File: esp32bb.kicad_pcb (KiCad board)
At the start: 2 copper layers, 43.2 x 61 mm, 33 parts, among them CON1 Micro_SD_Card, IC1 FT232RQ, J1 CONN_01X18, P1 CONN_01X17, P3 USB_OTG, Q1 MMBT3904, Q2 MMBT3904, SW1 SWITCH_SPST, SW2 SWITCH_SPST, U1 ESP32-WROOM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

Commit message: Update schema to use CP2102 and NCP1117DT33 and remove SD card holder
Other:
- board text added: "D00 PULL UP"
- board text removed: "D01 PULL UP"
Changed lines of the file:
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@@
     (effects (font (size 1.1 1.1) (thickness 0.2)))
   )
-  (gr_text "D01\nPULL\nUP" (at 161.417 118.237) (layer B.SilkS)
+  (gr_text "D00\nPULL\nUP" (at 161.417 118.237) (layer B.SilkS)
     (effects (font (size 0.7 0.7) (thickness 0.175)) (justify right mirror))
   )

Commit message: Update pcb for rev2.0
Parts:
- removed CON1: Micro_SD_Card, Connectors_Hirose:microSD_Card_Receptacle_Hirose_DM3AT-SF-PEJM5
- removed IC1: FT232RQ, ftdi232rq:FR232RQ
- removed J1: CONN_01X18, common:Pin_Header_Straight_1x18_Pitch2.54mm
- removed R10, R11, R12, R13, R8, R9: 10K, Resistors_SMD:R_0603
- added C1: 1nf, Capacitors_SMD:C_0603, F.Cu at (171.8, 101.8)
- added C7: 1nf, Capacitors_SMD:C_0603, F.Cu at (171.8, 94.6)
- added C8: 100uf, Capacitors_SMD:C_1206, F.Cu at (169.8, 106.3)
- added P2: CONN_01X17, common:Pin_Header_Straight_1x17_Pitch2.54mm, B.Cu at (190.5, 71.1)
- added P3: USB_OTG, usb_micro_b:USB_MICRO_B-HIROSE-ZX62R-B-5P, F.Cu at (167.6, 115.3)
- added U3: CP2102, Housings_DFN_QFN:QFN-28-1EP_5x5mm_Pitch0.5mm, F.Cu at (180.7, 100.4)
- D2: value D02 -> D05
- U2: value NJU7223DL1-33 -> NCP1117ST33T3G; footprint TO_SOT_Packages_SMD:TO-252-2Lead -> TO_SOT_Packages_SMD:SOT-223
- moved SW2 24.9 mm to (159.2, 118.8)
- moved SW1 24.9 mm to (184.1, 118.8)
- moved C4 23.5 mm to (162.0, 106.3)
- moved C5 23.5 mm to (162.0, 103.7)
- moved U2 19.5 mm to (164.1, 98.2)
- moved REF*** 18.6 mm to (157.4, 110.5)
- moved C2 16.3 mm to (165.4, 106.3), turned to 180 degrees
- moved C3 16.3 mm to (165.4, 103.7), turned to 180 degrees
- moved D1 12.8 mm to (174.5, 106.3), turned to 0 degrees
- moved D2 11.3 mm to (177.7, 119.1)
- moved R5 8.13 mm to (180.8, 95.4)
- moved R6 7.46 mm to (173.7, 98.1)
- moved Q1 6.11 mm to (174.5, 101.8)
- moved G*** 5.80 mm to (171.6, 65.9)
- moved U1 5.62 mm to (171.6, 76.5)
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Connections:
- C6 pad 1: Net-(C6-Pad1) -> GND
- C6 pad 2: GND -> Net-(C6-Pad2)
- P1 pad 17: +3V3 -> VCC
- R7 pad 1: IO2 -> IO5
- U1 pad 17: SD2 -> Net-(U1-Pad17)
- U1 pad 18: SD3 -> Net-(U1-Pad18)
- U1 pad 19: SD_CMD -> Net-(U1-Pad19)
- U1 pad 20: SD_CLK -> Net-(U1-Pad20)
- U1 pad 21: SD0 -> Net-(U1-Pad21)
- U1 pad 22: SD1 -> Net-(U1-Pad22)
- U2 pad 1: +3V3 -> GND
- U2 pad 2: VCC -> +3V3
- U2 pad 3: GND -> VCC
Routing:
- net GND: track 218.3 -> 291.8 mm, vias 11 -> 24
- net SD1: track 39.0 -> 0.00 mm
- net +3V3: track 151.9 -> 113.5 mm, vias 7 -> 4
- net SD0: track 36.4 -> 0.00 mm, vias 2 -> 0
- net SD_CLK: track 32.6 -> 0.00 mm, vias 2 -> 0
- net SD_CMD: track 28.0 -> 0.00 mm, vias 2 -> 0
- net SD3: track 26.6 -> 0.00 mm, vias 2 -> 0
- net SD2: track 25.5 -> 0.00 mm, vias 2 -> 0
- net Net-(P3-Pad4): track 0.00 -> 14.9 mm, vias 0 -> 2
- net IO2: track 39.5 -> 27.2 mm, vias 3 -> 0
- net IO5: track 21.3 -> 33.4 mm, vias 0 -> 1
- net D+: track 18.4 -> 29.1 mm, vias 0 -> 2
- net D-: track 18.5 -> 27.6 mm, vias 0 -> 2
- net IO0(boot): track 64.6 -> 57.5 mm, vias 4 -> 3
- net (no net): track 2.72 -> 9.74 mm, vias 0 -> 5
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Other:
- outline, holes or cut-outs redrawn
- board text added: "D00"
- board text added: "Rev 2.0"
- board text added: "VIN"
- board text removed: "D00 PULL UP"
- board text removed: "Rev 1.4"
- board text removed: "VCC"

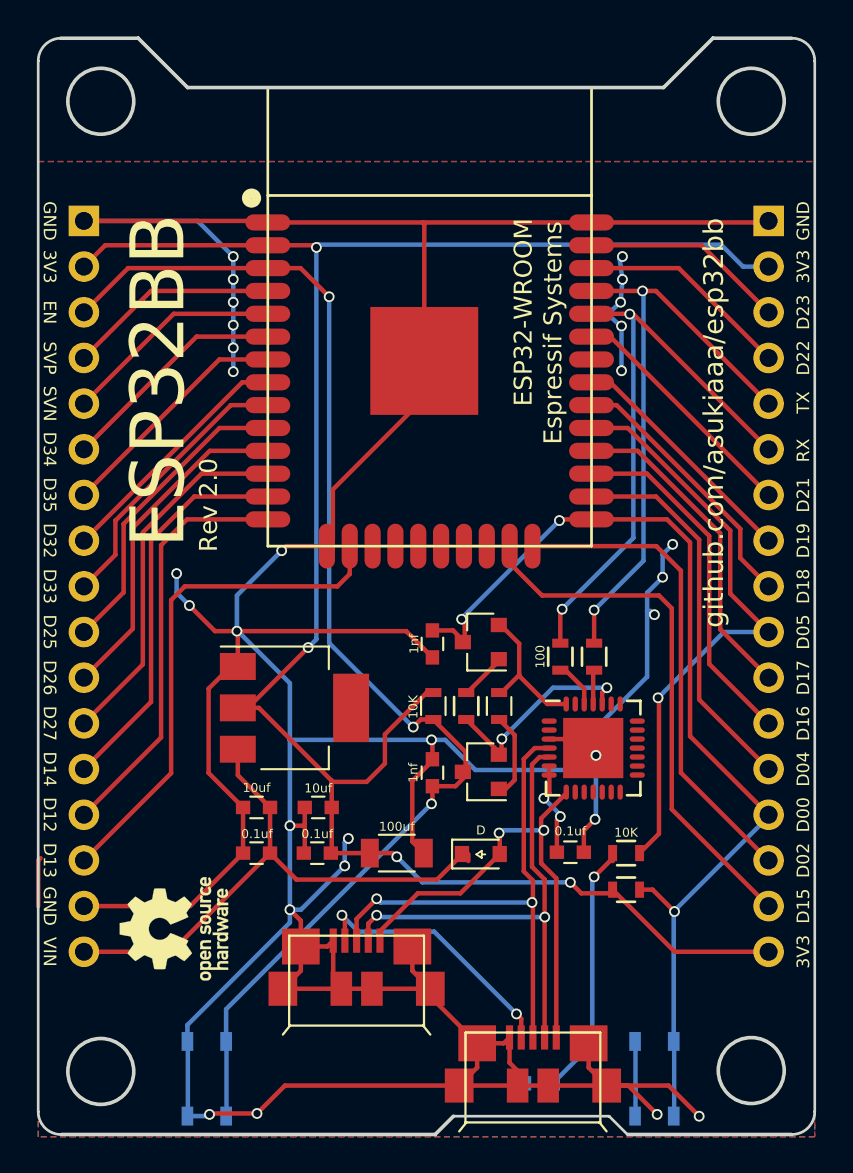
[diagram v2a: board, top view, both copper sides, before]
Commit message: Correct and update schema and pcb for rev2.1
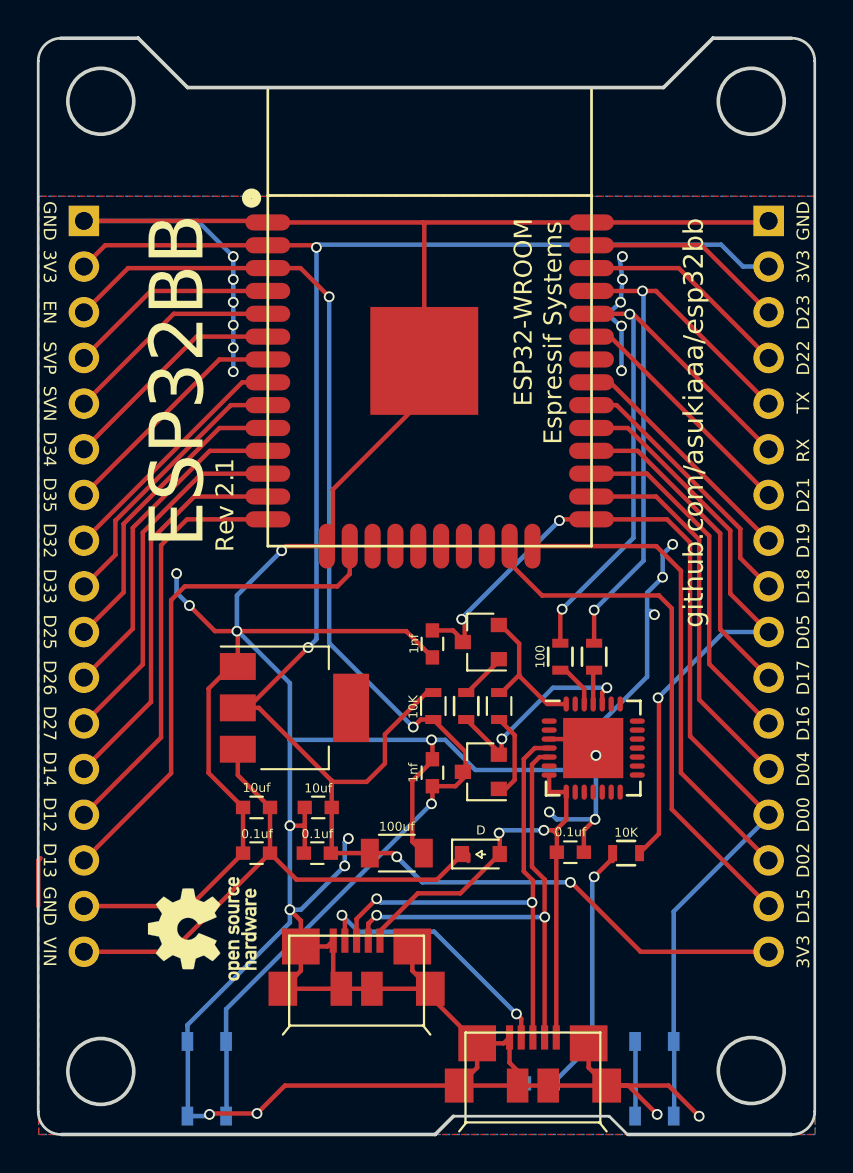
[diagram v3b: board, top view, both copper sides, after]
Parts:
- removed R2: 10K, Resistors_SMD:R_0603
- D2: value D05 -> D02
- moved REF*** 1.57 mm to (159.0, 110.5)
- turned C6 to 0 degrees
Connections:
- C6 pad 1: GND -> +5V
- C6 pad 2: Net-(C6-Pad2) -> GND
- U3 pad 6: Net-(C6-Pad2) -> Net-(U3-Pad6)
- U3 pad 7: Net-(C6-Pad2) -> +5V
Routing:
- net Net-(C6-Pad2): track 5.38 -> 0.00 mm, vias 2 -> 0
- net GND: track 291.8 -> 294.5 mm, vias 24 -> 25
- net IO0(boot): track 57.5 -> 55.0 mm, vias 3 -> 2
- net +5V: track 27.9 -> 30.0 mm
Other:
- board text added: "Rev 2.1"
- board text removed: "Rev 2.0"

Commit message: Correct led label to D05
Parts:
- D2: value D02 -> D05
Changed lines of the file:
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@@
     (links 109)
     (no_connects 0)
-    (area 149.784999 60.859999 193.115001 122.020001)
+    (area 138.257687 47.6936 217.291515 126.218342)
     (thickness 1.6)
     (drawings 102)
@@
       (effects (font (size 1 1) (thickness 0.15)) (justify mirror))
     )
-    (fp_text value D02 (at 0 1.1684) (layer B.SilkS)
+    (fp_text value D05 (at 0 1.1684) (layer B.SilkS)
       (effects (font (size 0.7 0.7) (thickness 0.175)) (justify mirror))
     )

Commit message: Modify ground zone
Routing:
- net GND: track 294.5 -> 360.6 mm, vias 25 -> 39
- net (no net): track 9.74 -> 2.72 mm, vias 5 -> 0
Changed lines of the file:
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@@
     (thickness 1.6)
     (drawings 102)
-    (tracks 487)
+    (tracks 511)
     (zones 0)
     (modules 29)
@@
   (gr_line (start 193.04 120.65) (end 193.04 62.23) (angle 90) (layer Edge.Cuts) (width 0.15))
   (gr_line (start 149.86 62.23) (end 149.86 120.65) (angle 90) (layer Edge.Cuts) (width 0.15))
-  (segment (start 182.3466 74.3712) (end 182.1942 73.2536) (width 0.25) (layer B.Cu) (net 0))
-  (via (at 182.3466 73.1012) (size 0.6) (drill 0.4) (layers F.Cu B.Cu) (net 0))
-  (segment (start 182.1942 73.2536) (end 182.3466 73.1012) (width 0.25) (layer B.Cu) (net 0))
   (segment (start 149.86 109.22) (end 149.86 106.68) (width 0.25) (layer F.Cu) (net 0))
   (segment (start 149.86 106.68) (end 149.987 106.553) (width 0.25) (layer F.Cu) (net 0))
-  (segment (start 182.245 75.6412) (end 182.3466 74.422) (width 0.25) (layer B.Cu) (net 0))
-  (segment (start 182.245 76.962) (end 181.6862 76.454) (width 0.25) (layer B.Cu) (net 0))
-  (segment (start 181.6862 76.454) (end 181.6862 76.1492) (width 0.25) (layer B.Cu) (net 0))
-  (segment (start 181.6862 76.1492) (end 182.245 75.6412) (width 0.25) (layer B.Cu) (net 0))
-  (via (at 182.245 75.6412) (size 0.6) (drill 0.4) (layers F.Cu B.Cu) (net 0))
-  (via (at 182.2958 79.4512) (size 0.6) (drill 0.4) (layers F.Cu B.Cu) (net 0))
-  (via (at 182.2958 76.962) (size 0.6) (drill 0.4) (layers F.Cu B.Cu) (net 0))
-  (segment (start 182.2958 79.4512) (end 182.2958 76.962) (width 0.25) (layer B.Cu) (net 0))
-  (segment (start 182.2958 76.962) (end 182.245 76.962) (width 0.25) (layer B.Cu) (net 0))
-  (segment (start 182.3466 74.3712) (end 182.2958 74.3712) (width 0.25) (layer F.Cu) (net 0))
-  (via (at 182.3466 74.3712) (size 0.6) (drill 0.4) (layers F.Cu B.Cu) (net 0))
-  (segment (start 182.3466 74.422) (end 182.3466 74.3712) (width 0.25) (layer B.Cu) (net 0))
   (segment (start 179.451 107.8992) (end 179.5018 107.8992) (width 0.25) (layer F.Cu) (net 1))
   (via (at 179.451 107.8992) (size 0.6) (drill 0.4) (layers F.Cu B.Cu) (net 1))
@@
   (segment (start 190.5 73.66) (end 190.373 73.66) (width 0.25) (layer B.Cu) (net 1))
   (segment (start 166.2938 106.4126) (end 166.1548 106.2736) (width 0.25) (layer F.Cu) (net 1))
+  (segment (start 152.4 71.12) (end 152.781 71.12) (width 0.25) (layer B.Cu) (net 2))
+  (segment (start 152.781 71.12) (end 154.051 69.85) (width 0.25) (layer B.Cu) (net 2))
+  (segment (start 190.4746 70.0024) (end 190.4746 71.12) (width 0.25) (layer B.Cu) (net 2))
+  (segment (start 190.627 69.85) (end 190.4746 70.0024) (width 0.25) (layer B.Cu) (net 2))
+  (via (at 190.627 69.85) (size 0.6) (drill 0.4) (layers F.Cu B.Cu) (net 2))
+  (segment (start 185.547 69.85) (end 190.627 69.85) (width 0.25) (layer F.Cu) (net 2))
+  (via (at 185.547 69.85) (size 0.6) (drill 0.4) (layers F.Cu B.Cu) (net 2))
+  (segment (start 180.467 69.85) (end 185.547 69.85) (width 0.25) (layer B.Cu) (net 2))
+  (via (at 180.467 69.85) (size 0.6) (drill 0.4) (layers F.Cu B.Cu) (net 2))
+  (segment (start 175.387 69.85) (end 180.467 69.85) (width 0.25) (layer F.Cu) (net 2))
+  (via (at 175.387 69.85) (size 0.6) (drill 0.4) (layers F.Cu B.Cu) (net 2))
+  (segment (start 169.799 69.85) (end 175.387 69.85) (width 0.25) (layer B.Cu) (net 2))
+  (via (at 169.799 69.85) (size 0.6) (drill 0.4) (layers F.Cu B.Cu) (net 2))
+  (segment (start 164.211 69.85) (end 169.799 69.85) (width 0.25) (layer F.Cu) (net 2))
+  (via (at 164.211 69.85) (size 0.6) (drill 0.4) (layers F.Cu B.Cu) (net 2))
+  (segment (start 159.131 69.85) (end 164.211 69.85) (width 0.25) (layer B.Cu) (net 2))
+  (via (at 159.131 69.85) (size 0.6) (drill 0.4) (layers F.Cu B.Cu) (net 2))
+  (segment (start 154.051 69.85) (end 159.131 69.85) (width 0.25) (layer F.Cu) (net 2))
+  (via (at 154.051 69.85) (size 0.6) (drill 0.4) (layers F.Cu B.Cu) (net 2))
+  (segment (start 182.2958 73.1012) (end 182.2958 74.3712) (width 0.25) (layer B.Cu) (net 2))
+  (segment (start 182.245 74.422) (end 182.2958 74.3712) (width 0.25) (layer B.Cu) (net 2))
+  (via (at 182.2958 74.3712) (size 0.6) (drill 0.4) (layers F.Cu B.Cu) (net 2))
+  (segment (start 181.6862 76.4032) (end 182.2958 77.0128) (width 0.25) (layer B.Cu) (net 2))
+  (via (at 182.245 75.6412) (size 0.6) (drill 0.4) (layers F.Cu B.Cu) (net 2))
+  (segment (start 181.6862 76.2) (end 182.245 75.6412) (width 0.25) (layer B.Cu) (net 2))
+  (segment (start 181.6862 76.4032) (end 181.6862 76.2) (width 0.25) (layer B.Cu) (net 2))
+  (segment (start 182.245 75.6412) (end 182.245 74.422) (width 0.25) (layer B.Cu) (net 2))
+  (via (at 182.2958 73.1012) (size 0.6) (drill 0.4) (layers F.Cu B.Cu) (net 2))
+  (segment (start 182.2958 79.4512) (end 182.2958 77.0128) (width 0.25) (layer B.Cu) (net 2))
+  (segment (start 181.737 87.5284) (end 181.737 87.6808) (width 0.25) (layer B.Cu) (net 2))
+  (segment (start 181.737 87.6808) (end 182.2958 87.122) (width 0.25) (layer B.Cu) (net 2))
+  (segment (start 182.2958 87.122) (end 182.2958 79.4512) (width 0.25) (layer B.Cu) (net 2))
+  (via (at 182.2958 79.4512) (size 0.6) (drill 0.4) (layers F.Cu B.Cu) (net 2))
+  (segment (start 184.5818 90.932) (end 178.943 90.932) (width 0.25) (layer F.Cu) (net 2))
+  (via (at 178.6382 90.6272) (size 0.6) (drill 0.4) (layers F.Cu B.Cu) (net 2))
+  (segment (start 178.943 90.932) (end 178.6382 90.6272) (width 0.25) (layer F.Cu) (net 2))
+  (segment (start 178.6382 90.6272) (end 181.737 87.5284) (width 0.25) (layer B.Cu) (net 2))
+  (segment (start 182.2958 77.0128) (end 182.2958 77.0636) (width 0.25) (layer F.Cu) (net 2))
+  (via (at 182.2958 77.0128) (size 0.6) (drill 0.4) (layers F.Cu B.Cu) (net 2))
   (segment (start 180.8226 104.394) (end 178.689 104.394) (width 0.25) (layer B.Cu) (net 2))
   (via (at 178.2826 103.9876) (size 0.6) (drill 0.4) (layers F.Cu B.Cu) (net 2))

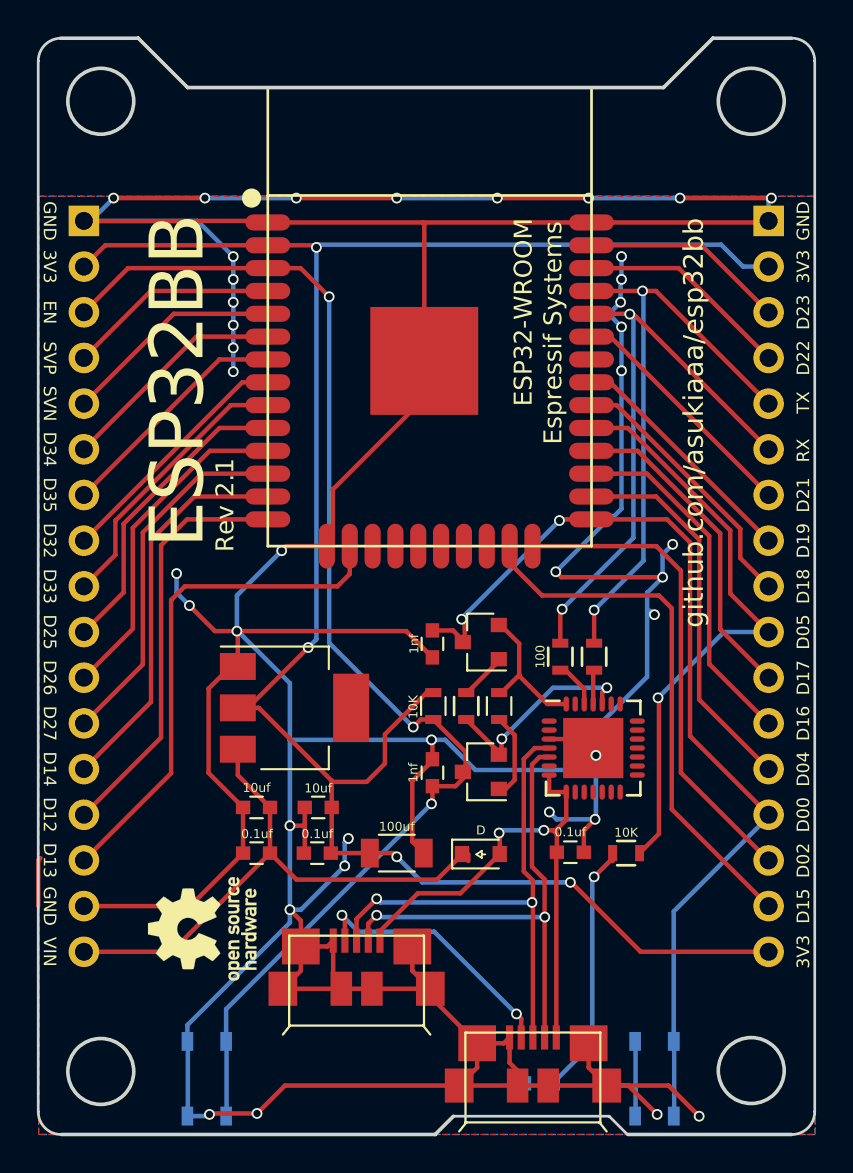
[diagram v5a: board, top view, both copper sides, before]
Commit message: Add diode for 3v3 and modify label for registers and condensors
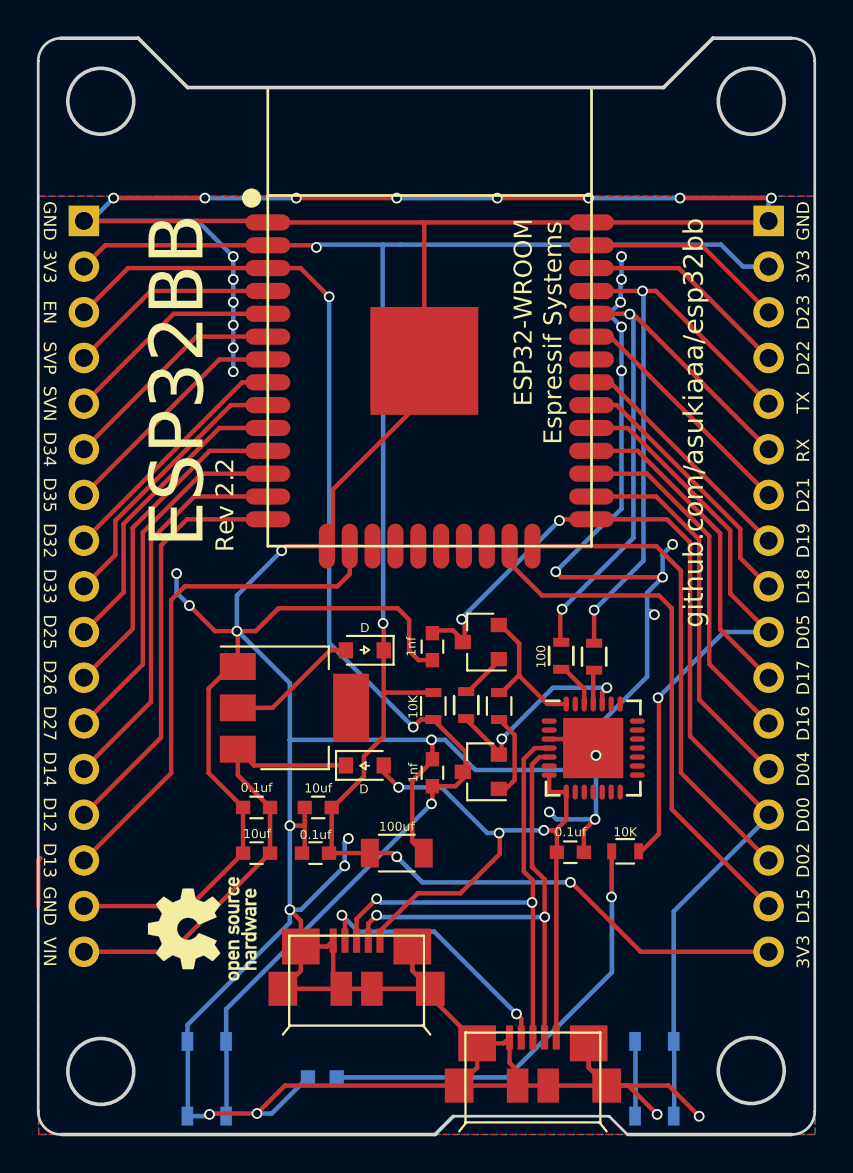
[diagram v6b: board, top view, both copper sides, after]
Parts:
- removed R7: 10K, Resistors_SMD:R_0603
- added D3: D05, LEDs:LED_0603, B.Cu at (165.7, 118.7)
- added R2: 10K, Resistors_SMD:R_0603, F.Cu at (182.5, 106.2)
- C2: value 0.1uf -> 1nf
- C4: value 0.1uf -> 10uf
- C5: value 10uf -> 0.1uf
- C7: value 1nf -> 0.1uf
- D2: value D05 -> D; footprint common:LED_0603 -> common:D_0805; moved to F.Cu
- R4: value 100 -> 10K
- R6: value 10K -> 100
- moved D2 25.9 mm to (168.0, 95.0), turned to 180 degrees
- moved C7 13.3 mm to (165.3, 106.3), turned to 180 degrees
- moved C2 13.1 mm to (171.8, 94.8), turned to 270 degrees
- moved D1 8.12 mm to (168.0, 101.4)
- moved R6 5.98 mm to (178.9, 95.3), turned to 270 degrees
- moved R4 5.88 mm to (173.7, 98.0), turned to 90 degrees
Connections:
- C2 pad 1: +3V3 -> IO0(boot)
- C7 pad 1: IO0(boot) -> +3V3
- D2 pad 1: GND -> +3V3
- R4 pad 1: TXDtoRXD0 -> RTS
- R4 pad 2: Net-(R4-Pad2) -> Net-(Q2-Pad1)
- R6 pad 1: RTS -> TXDtoRXD0
- R6 pad 2: Net-(Q2-Pad1) -> Net-(R6-Pad2)
- U2 pad 2: +3V3 -> Net-(D2-Pad2)
- U3 pad 26: Net-(R4-Pad2) -> Net-(R6-Pad2)
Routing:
- net Net-(D3-Pad2): track 0.00 -> 24.7 mm, vias 0 -> 1
- net +3V3: track 113.4 -> 104.3 mm
- net +5V: track 30.0 -> 38.2 mm, vias 2 -> 3
- net Net-(D2-Pad2): track 15.3 -> 7.90 mm, vias 1 -> 0
- net VCC: track 31.4 -> 25.5 mm
- net GND: track 360.6 -> 366.4 mm
- net Net-(R6-Pad2): track 0.00 -> 2.60 mm
- net Net-(R4-Pad2): track 2.60 -> 0.00 mm
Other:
- board text added: "Rev 2.2"
- board text removed: "Rev 2.1"
